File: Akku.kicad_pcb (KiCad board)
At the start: 2 copper layers, 100 x 160 mm, 53 parts, among them J1 +/- Stecker, J2 load/up, J3 down/en/clear, P7 CONN_02X10, P8 CONN_02X10, P9 CONN_02X10, SW1 UP_Bonsai_SWITCH_INV, SW2 DOWN_Bonsai_SWITCH_INV, SW3 CLR_Bonsai_SWITCH_INV, U1 74HC14, U2 7400, U4 7408, U5 74LS193, U6 74LS541, U7 74LS193, U8 74LS540

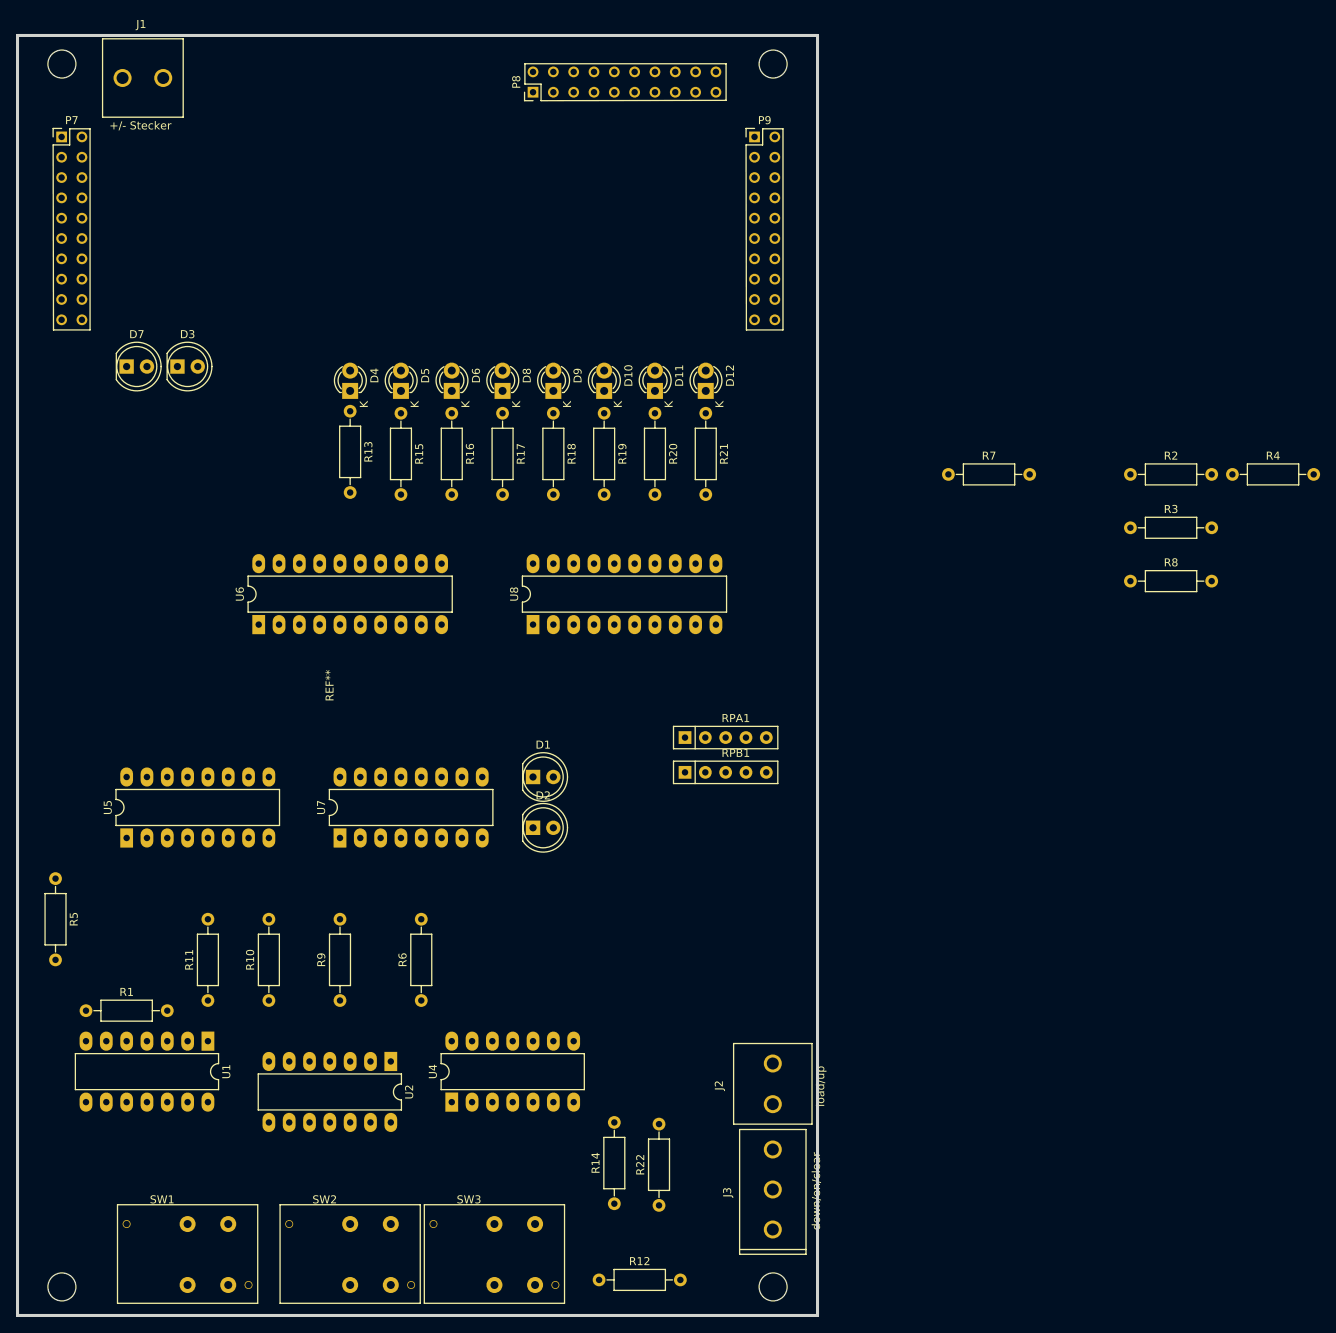
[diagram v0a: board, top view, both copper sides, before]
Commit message: akku unit changing labeling rpack
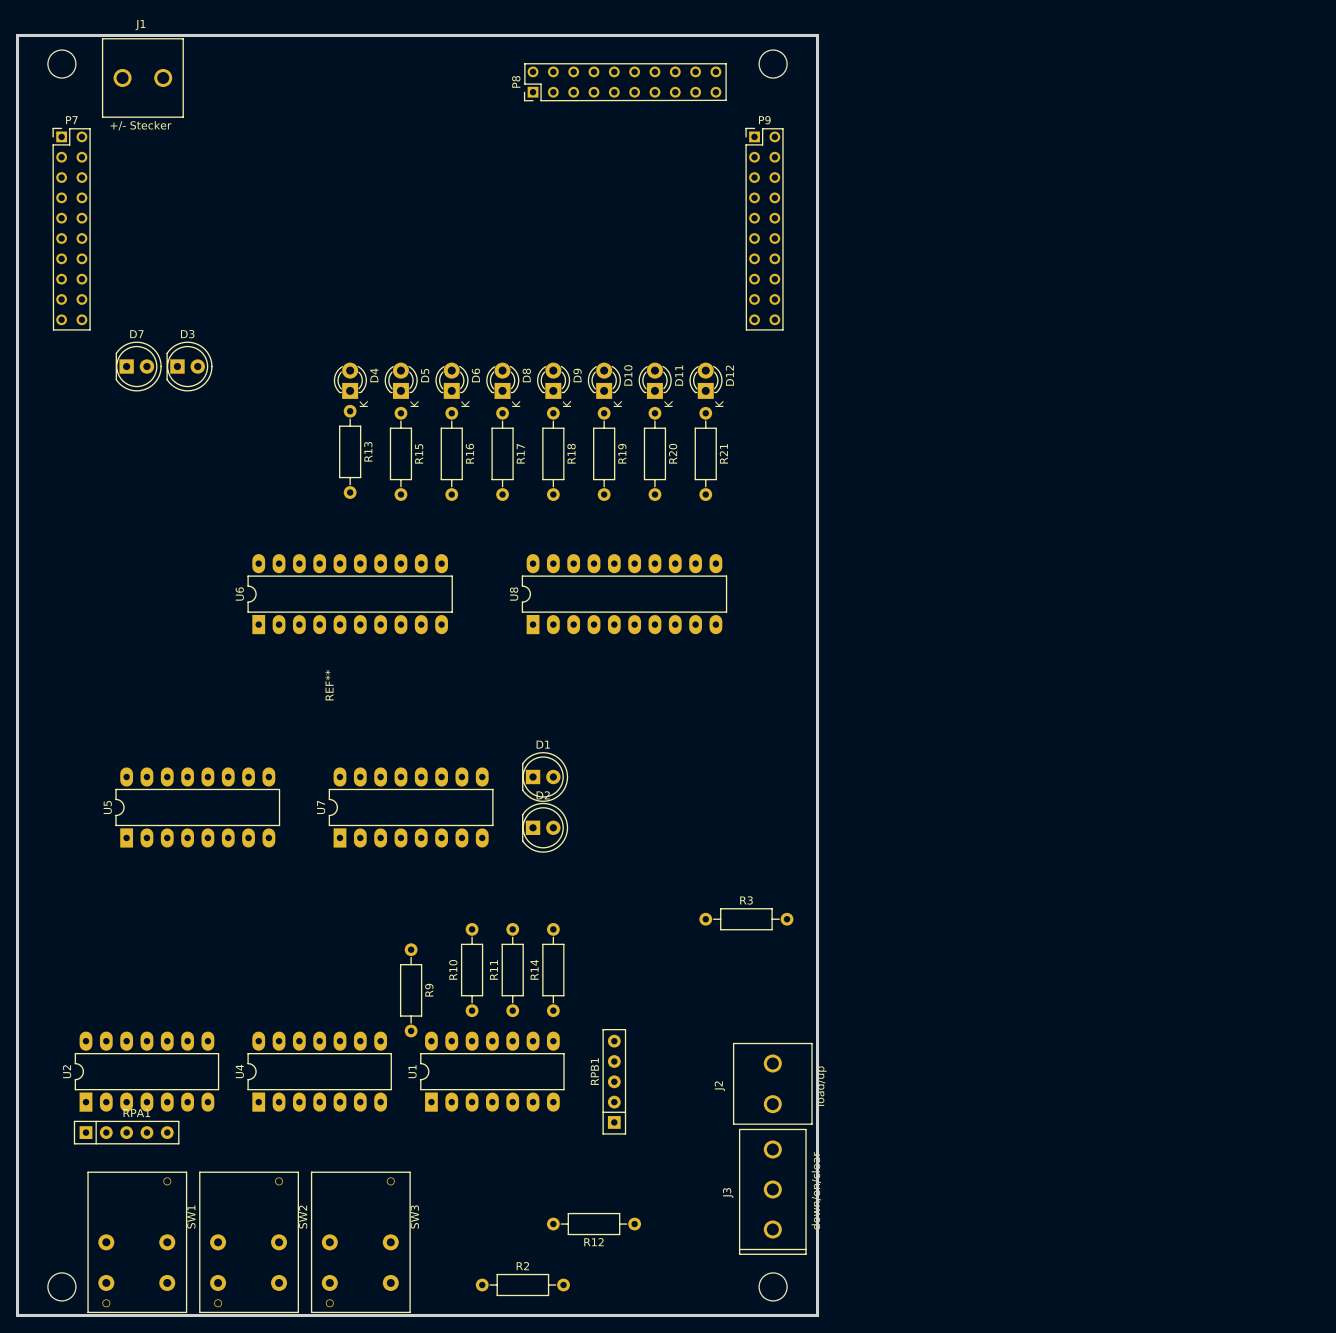
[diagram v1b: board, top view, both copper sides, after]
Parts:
- removed R1, R22, R4, R5, R6, R7, R8: R, Resistors_ThroughHole:R_Axial_DIN0207_L6.3mm_D2.5mm_P10.16mm_Horizontal
- removed the REF** at (139.7, 237.5)
- added REF**: EuroBoard160mmX100mm_holes, tg_foodprint:EuroBoard160mmX100mm_holes, F.Cu at (139.7, 237.5)
- moved R2 129.7 mm to (97.8, 233.7)
- moved RPA1 89.7 mm to (48.3, 214.6)
- moved R3 72.2 mm to (125.7, 188.0)
- moved RPB1 44.6 mm to (114.3, 213.4), turned to 90 degrees
- moved U2 38.4 mm to (48.3, 210.8), turned to 90 degrees
- moved R11 38.1 mm to (101.6, 199.4)
- moved U1 29.0 mm to (91.4, 210.8), turned to 90 degrees
- moved R10 25.4 mm to (96.5, 199.4)
- moved R14 25.3 mm to (106.7, 199.4)
- moved U4 24.1 mm to (69.8, 210.8)
- moved SW3 13.2 mm to (86.4, 228.3), turned to 270 degrees
- moved R9 10.9 mm to (88.9, 191.8), turned to 270 degrees
- moved SW2 9.18 mm to (72.4, 228.3), turned to 270 degrees
- moved R12 8.28 mm to (116.8, 226.1), turned to 180 degrees
- moved SW1 3.42 mm to (58.4, 228.3), turned to 270 degrees
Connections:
- D1 pad 1: Net-(D1-Pad1) -> GND
- J2 pad 1: Net-(J2-Pad1) -> RPB4
- J3 pad 1: RPAVCC -> RPB2
- J3 pad 2: Net-(J3-Pad2) -> RPB3
- R9 pad 1: Net-(D1-Pad1) -> Net-(D1-Pad2)
- R9 pad 2: GND -> Net-(R9-Pad2)
- RPA1 pad 2: (no net) -> RPA1
- RPA1 pad 4: (no net) -> RPA3
- RPA1 pad 5: (no net) -> RPA4
- RPB1 pad 1: (no net) -> VCC
- RPB1 pad 2: RPB -> (no net)
- RPB1 pad 3: RPB -> RPB2
- RPB1 pad 4: RPB -> RPB3
- RPB1 pad 5: RPB -> RPB4
- SW1 pad 1: Net-(R5-Pad2) -> RPA2
- SW1 pad 2: Net-(R4-Pad2) -> RPA1
- SW2 pad 1: Net-(R6-Pad1) -> RPA4
- SW2 pad 2: RPA2 -> RPA3
- U1 pad 6: Net-(D1-Pad2) -> Net-(R9-Pad2)
- U1 pad 9: Net-(J2-Pad1) -> RPB4
- U2 pad 1: Net-(R4-Pad2) -> RPA1
- U2 pad 10: Net-(R6-Pad1) -> RPA4
- U2 pad 12: RPA2 -> Net-(U2-Pad12)
- U2 pad 13: Net-(U2-Pad13) -> RPA2
- U2 pad 2: Net-(U2-Pad2) -> Net-(U2-Pad11)
- U2 pad 3: Net-(U2-Pad3) -> Net-(U2-Pad12)
- U2 pad 4: Net-(U2-Pad3) -> RPA3
- U2 pad 5: Net-(R5-Pad2) -> Net-(U2-Pad5)
- U2 pad 6: Net-(U2-Pad2) -> Net-(U2-Pad6)
- U2 pad 8: Net-(U2-Pad13) -> Net-(U2-Pad5)
- U2 pad 9: Net-(U2-Pad11) -> Net-(U2-Pad6)
- U4 pad 1: Net-(J3-Pad2) -> Net-(U2-Pad5)
- U4 pad 11: Net-(U1-Pad13) -> Net-(U1-Pad11)
- U4 pad 12: Net-(U2-Pad13) -> RPB3
- U4 pad 13: RPAVCC -> Net-(U2-Pad12)
- U4 pad 2: Net-(U2-Pad3) -> RPB2
- U4 pad 3: Net-(U1-Pad11) -> Net-(U1-Pad13)
- U5 pad 11: Net-(J2-Pad1) -> RPB4
- U7 pad 11: Net-(J2-Pad1) -> RPB4

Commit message: akku sch updates for same wireing in pcb
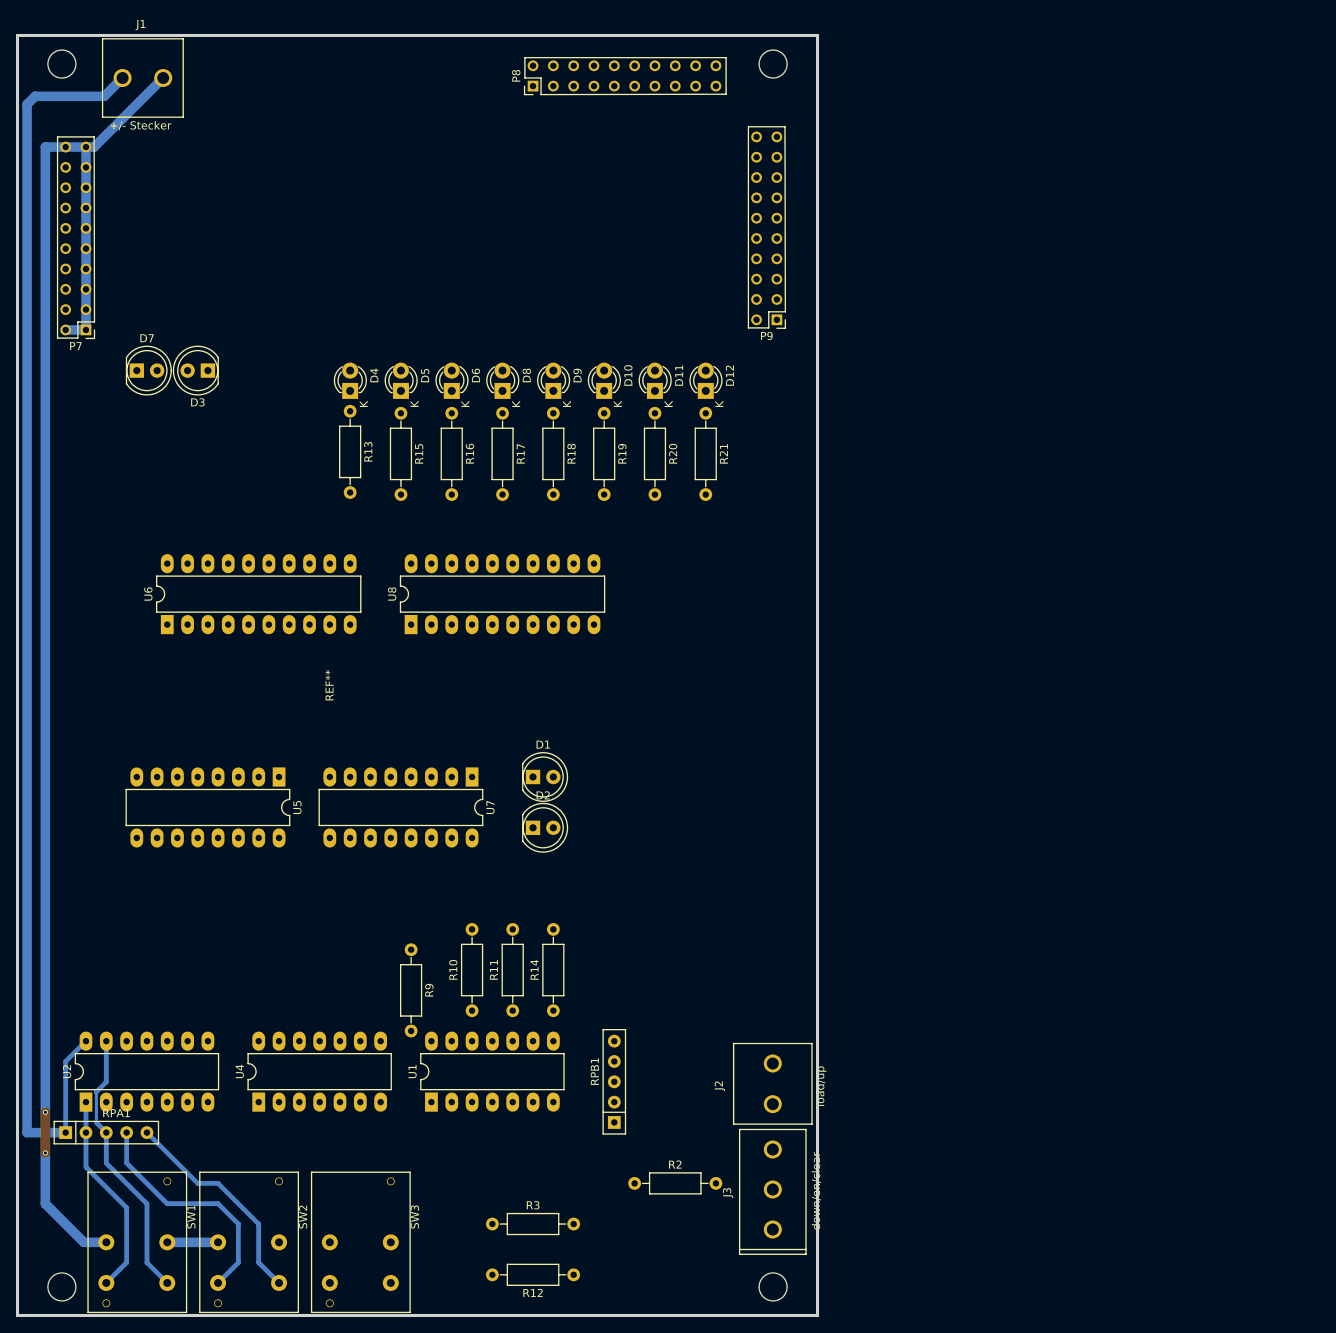
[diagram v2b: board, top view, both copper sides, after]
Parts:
- moved R3 46.5 mm to (99.1, 226.1)
- moved P7 24.3 mm to (48.3, 114.3), turned to 180 degrees
- moved P9 23.0 mm to (134.6, 113.0), turned to 180 degrees
- moved R2 22.9 mm to (116.8, 221.0)
- moved U5 20.5 mm to (72.4, 170.2), turned to 270 degrees
- moved U7 18.2 mm to (96.5, 170.2), turned to 270 degrees
- moved U8 15.2 mm to (88.9, 151.1)
- moved U6 11.4 mm to (58.4, 151.1)
- moved R12 9.92 mm to (109.2, 232.4)
- moved D3 3.84 mm to (63.5, 119.4), turned to 180 degrees
- moved RPA1 2.54 mm to (45.7, 214.6)
- moved D7 1.37 mm to (54.6, 119.4)
- moved P8 0.76 mm to (104.1, 83.8)
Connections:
- J2 pad 2: Net-(J2-Pad2) -> RPB3
- J3 pad 2: RPB3 -> ^enable
- J3 pad 3: Net-(J3-Pad3) -> CLR
- P7 pad 1: (no net) -> GND
- P7 pad 10: (no net) -> GND
- P7 pad 2: (no net) -> GND
- P7 pad 3: (no net) -> GND
- P7 pad 4: (no net) -> GND
- P7 pad 5: (no net) -> GND
- P7 pad 6: (no net) -> GND
- P7 pad 7: (no net) -> GND
- P7 pad 8: (no net) -> GND
- P7 pad 9: (no net) -> GND
- P8 pad 1: (no net) -> GND
- P8 pad 10: (no net) -> GND
- P8 pad 2: (no net) -> GND
- P8 pad 3: (no net) -> GND
- P8 pad 4: (no net) -> GND
- P8 pad 5: (no net) -> GND
- P8 pad 6: (no net) -> GND
- P8 pad 7: (no net) -> GND
- P8 pad 8: (no net) -> GND
- P8 pad 9: (no net) -> GND
- P9 pad 10: (no net) -> GND
- P9 pad 2: (no net) -> GND
- P9 pad 3: (no net) -> GND
- P9 pad 4: (no net) -> GND
- P9 pad 5: (no net) -> GND
- P9 pad 6: (no net) -> GND
- P9 pad 7: (no net) -> GND
- P9 pad 8: (no net) -> GND
- P9 pad 9: (no net) -> GND
- R12 pad 1: Net-(J2-Pad2) -> CLR
- R2 pad 2: Net-(J3-Pad3) -> ^enable
- R3 pad 2: Net-(J3-Pad3) -> ^enable
- SW1 pad 1: RPA2 -> RPA1
- SW1 pad 2: RPA1 -> RPA2
- SW2 pad 1: RPA4 -> RPA3
- SW2 pad 2: RPA3 -> RPA4
- U1 pad 1: Net-(J3-Pad3) -> ^enable
- U5 pad 1: Net-(U5-Pad1) -> /a2
- U5 pad 10: Net-(U5-Pad10) -> /a1
- U5 pad 14: Net-(J2-Pad2) -> CLR
- U5 pad 15: Net-(U5-Pad15) -> /a3
- U5 pad 9: Net-(U5-Pad9) -> /a0
- U6 pad 11: Net-(U6-Pad11) -> /a7
- U6 pad 12: Net-(U6-Pad12) -> /a6
- U6 pad 13: Net-(U6-Pad13) -> /a5
- U6 pad 14: Net-(U6-Pad14) -> /a4
- U6 pad 15: Net-(U5-Pad9) -> /a3
- U6 pad 16: Net-(U5-Pad10) -> /a2
- U6 pad 17: Net-(U5-Pad1) -> /a1
- U6 pad 18: Net-(U5-Pad15) -> /a0
- U6 pad 2: Net-(U5-Pad2) -> Net-(U5-Pad7)
- U6 pad 3: Net-(U5-Pad3) -> Net-(U5-Pad6)
- U6 pad 4: Net-(U5-Pad7) -> Net-(U5-Pad2)
- U6 pad 5: Net-(U5-Pad6) -> Net-(U5-Pad3)
- U7 pad 1: Net-(U6-Pad13) -> /a6
- U7 pad 10: Net-(U6-Pad12) -> /a5
- U7 pad 14: Net-(J2-Pad2) -> CLR
- U7 pad 15: Net-(U6-Pad14) -> /a7
- U7 pad 2: Net-(U6-Pad6) -> Net-(U6-Pad8)
- U7 pad 3: Net-(U6-Pad7) -> Net-(U6-Pad9)
- U7 pad 6: Net-(U6-Pad9) -> Net-(U6-Pad7)
- U7 pad 7: Net-(U6-Pad8) -> Net-(U6-Pad6)
- U7 pad 9: Net-(U6-Pad11) -> /a4
- U8 pad 2: Net-(U5-Pad2) -> Net-(U5-Pad7)
- U8 pad 3: Net-(U5-Pad3) -> Net-(U5-Pad6)
- U8 pad 4: Net-(U5-Pad7) -> Net-(U5-Pad2)
- U8 pad 5: Net-(U5-Pad6) -> Net-(U5-Pad3)
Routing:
- net GND: track 0.00 -> 191.8 mm, vias 0 -> 2
- net VCC: track 0.00 -> 159.1 mm
- net RPA2: track 0.00 -> 34.5 mm
- net RPA3: track 0.00 -> 29.4 mm
- net RPA4: track 0.00 -> 27.1 mm
- net RPA1: track 0.00 -> 25.8 mm
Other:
- net class Default: trace_width 0.4 -> 0.6
- net class Power added: clearance 0.4, trace_width 1.2, via_dia 0.6, via_drill 0.4
- net class smal added: clearance 0.2, trace_width 0.4, via_dia 0.6, via_drill 0.4

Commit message: akku wireing in pcb
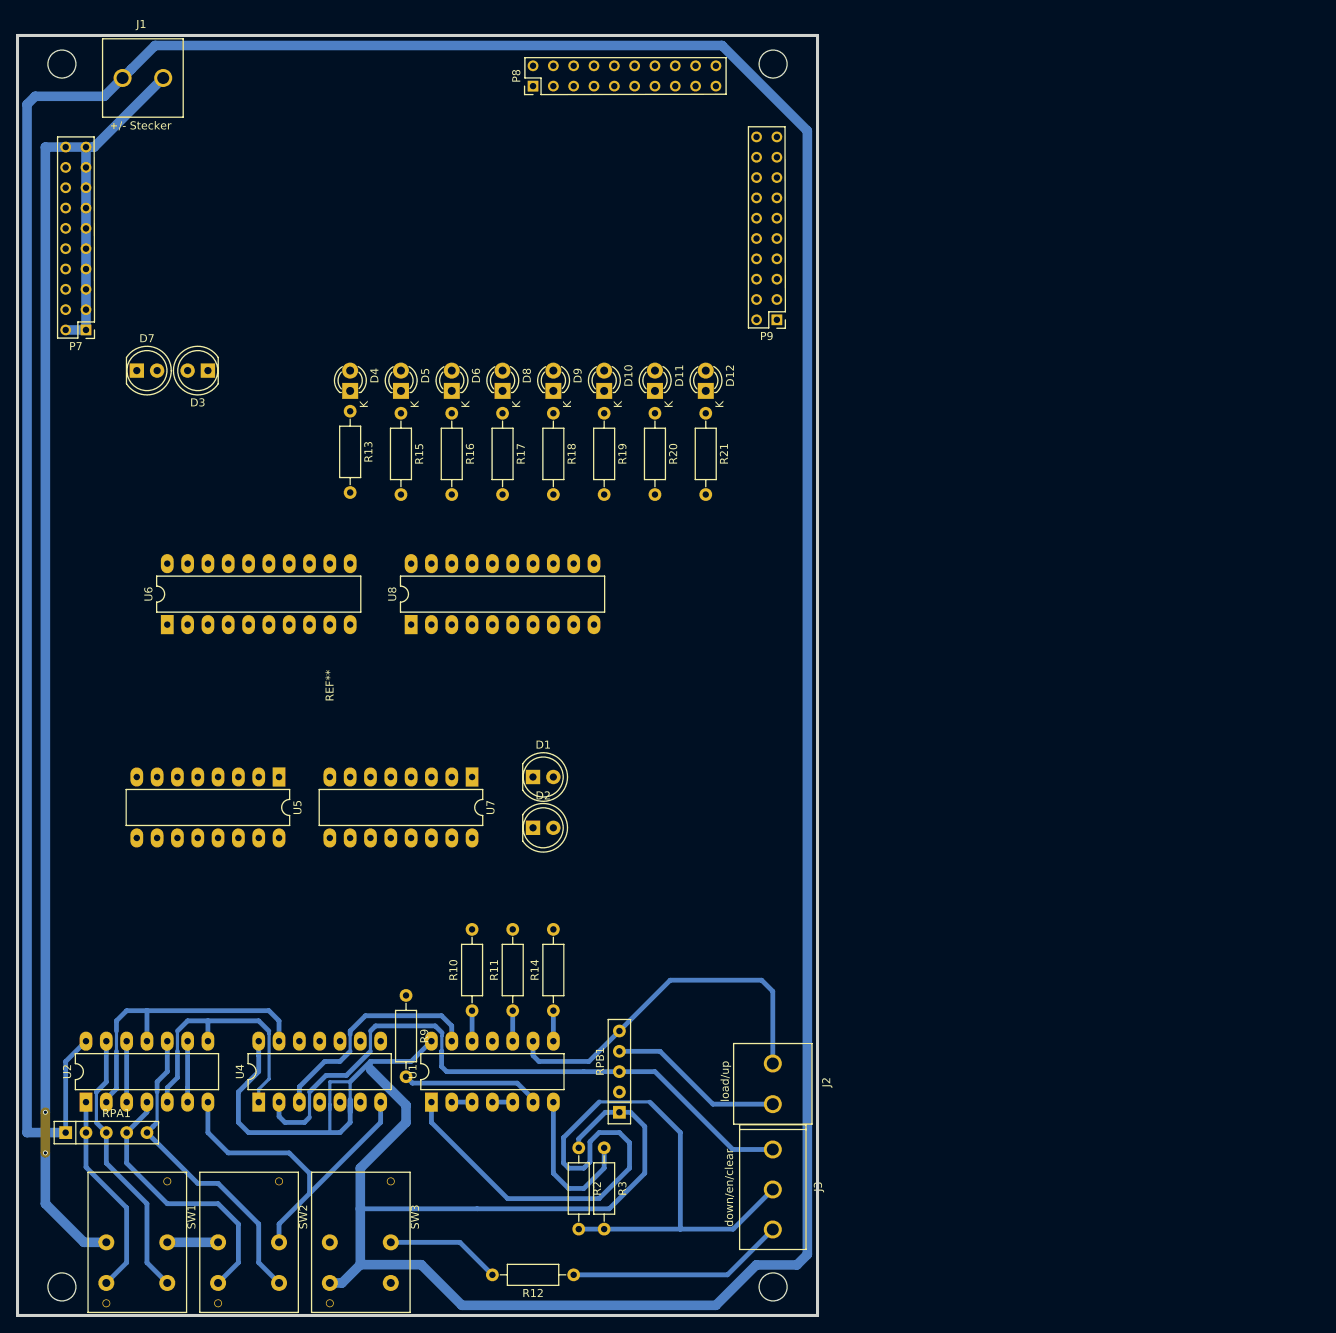
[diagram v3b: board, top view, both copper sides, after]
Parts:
- moved R3 16.9 mm to (113.0, 216.5), turned to 270 degrees
- moved R2 8.28 mm to (109.9, 216.5), turned to 270 degrees
- moved R9 5.75 mm to (88.3, 197.5)
- moved RPB1 1.42 mm to (114.9, 212.1)
- turned J2 to 270 degrees
- turned J3 to 270 degrees
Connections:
- U4 pad 13: Net-(U2-Pad12) -> Net-(U2-Pad11)
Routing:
- net VCC: track 159.1 -> 595.8 mm
- net ^enable: track 0.00 -> 108.0 mm
- net RPB2: track 0.00 -> 81.1 mm
- net GND: track 191.8 -> 255.3 mm
- net RPB4: track 0.00 -> 45.9 mm
- net Net-(U2-Pad11): track 0.00 -> 38.4 mm
- net Net-(U2-Pad5): track 0.00 -> 33.9 mm
- net Net-(U1-Pad13): track 0.00 -> 28.6 mm
- net CLR: track 0.00 -> 27.2 mm
- net RPB3: track 0.00 -> 21.9 mm
- net Net-(R9-Pad2): track 0.00 -> 17.4 mm
- net Net-(R12-Pad2): track 0.00 -> 14.4 mm
- net RPA4: track 27.1 -> 39.6 mm
- net Net-(U2-Pad6): track 0.00 -> 7.62 mm
- net Net-(U2-Pad12): track 0.00 -> 7.62 mm
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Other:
- net class Power: clearance 0.4 -> 0.3
